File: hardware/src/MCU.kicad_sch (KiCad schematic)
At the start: 15 parts, among them U201 ESP32-C3-WROOM-02, U202 TLV1117LV33

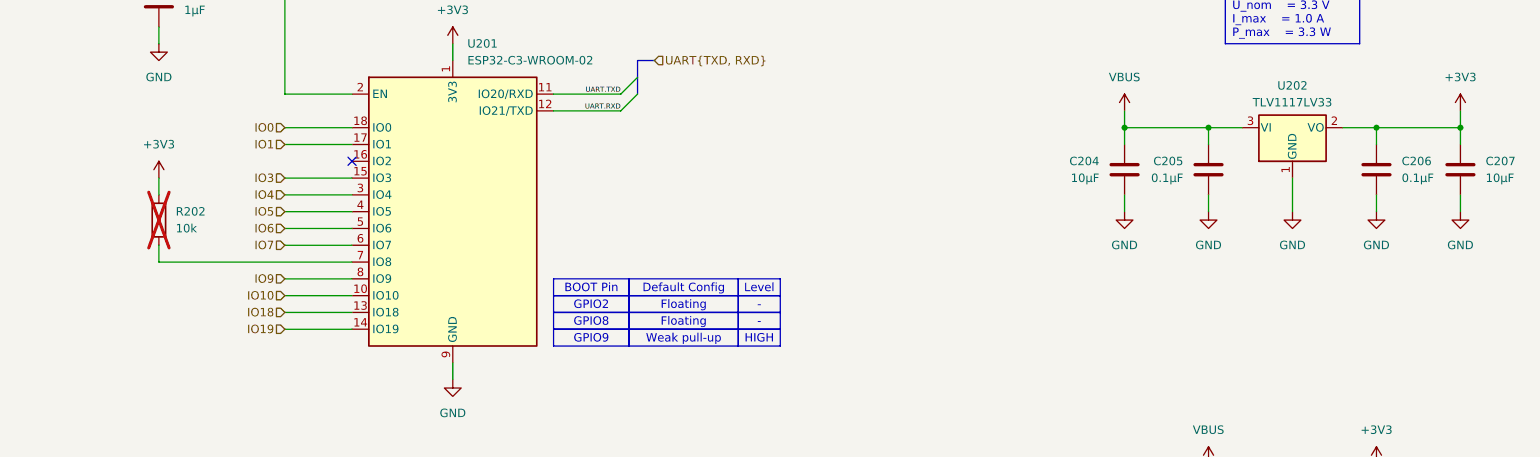
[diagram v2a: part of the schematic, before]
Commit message: Add: RTC schematic
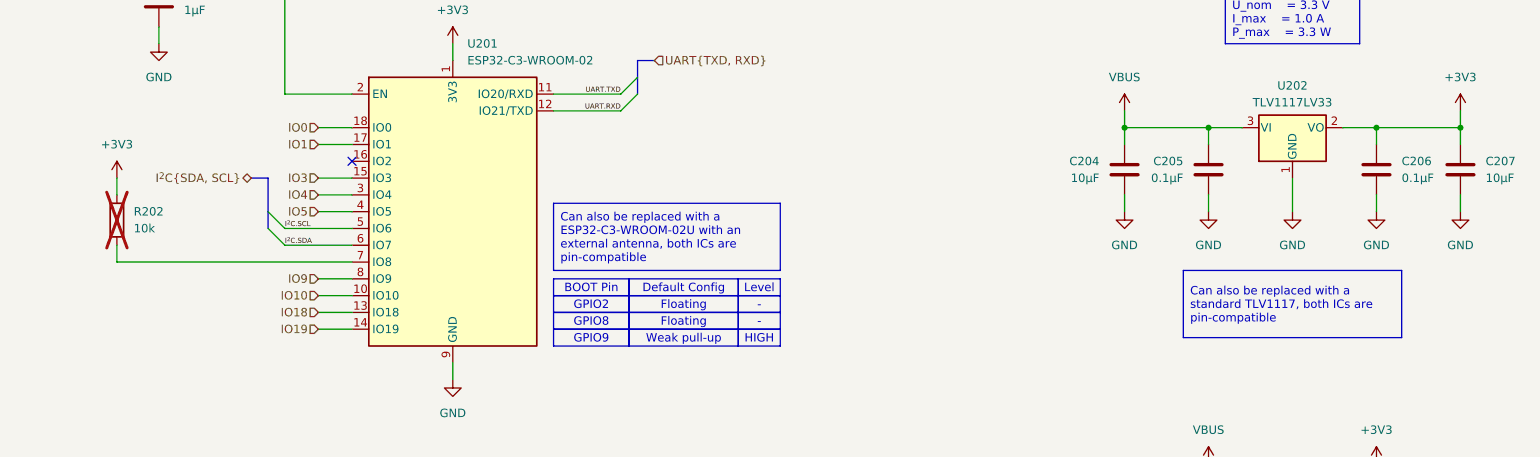
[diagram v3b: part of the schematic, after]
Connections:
- net IO6 renamed I^{2}C.SCL
- net IO7 renamed I^{2}C.SDA
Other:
- moved on the sheet: R202
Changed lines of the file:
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@@
+	)
+	(bus_entry
+		(at 60.96 78.74)
+		(size 2.54 2.54)
+		(stroke
+			(width 0)
+			(type default)
+		)
 	)
 	(bus_entry
@@
 		)
 	)
+	(bus_entry
+		(at 60.96 76.2)
+		(size 2.54 2.54)
+		(stroke
+			(width 0)
+			(type default)
+		)
+	)
 	(wire
 		(pts
@@
 	(wire
 		(pts
-			(xy 44.45 73.66) (xy 44.45 71.12)
+			(xy 38.1 73.66) (xy 38.1 71.12)
 		)
 		(stroke
@@
 		)
 	)
+	(bus
+		(pts
+			(xy 60.96 76.2) (xy 60.96 71.12)
+		)
+		(stroke
+			(width 0)
+			(type default)
+		)
+	)
 	(wire
 		(pts
@@
 		)
 	)
+	(bus
+		(pts
+			(xy 60.96 78.74) (xy 60.96 76.2)
+		)
+		(stroke
+			(width 0)
+			(type default)
+		)
+	)
 	(wire
 		(pts
@@
 	(wire
 		(pts
-			(xy 63.5 76.2) (xy 73.66 76.2)
-		)
-		(stroke
-			(width 0)
-			(type default)
-		)
-	)
-	(wire
-		(pts
-			(xy 63.5 73.66) (xy 73.66 73.66)
+			(xy 68.58 76.2) (xy 73.66 76.2)
+		)
+		(stroke
+			(width 0)
+			(type default)
+		)
+	)
+	(wire
+		(pts
+			(xy 68.58 73.66) (xy 73.66 73.66)
 		)
 		(stroke
@@
 	(wire
 		(pts
-			(xy 63.5 93.98) (xy 73.66 93.98)
+			(xy 68.58 93.98) (xy 73.66 93.98)
 		)
 		(stroke
@@
 	(wire
 		(pts
-			(xy 63.5 86.36) (xy 73.66 86.36)
+			(xy 68.58 86.36) (xy 73.66 86.36)
 		)
 		(stroke
@@
 	(wire
 		(pts
-			(xy 63.5 63.5) (xy 73.66 63.5)
+			(xy 68.58 63.5) (xy 73.66 63.5)
 		)
 		(stroke
@@
 	(wire
 		(pts
-			(xy 63.5 66.04) (xy 73.66 66.04)
+			(xy 68.58 66.04) (xy 73.66 66.04)
 		)
 		(stroke
@@
 		)
 	)
-	(wire
-		(pts
-			(xy 44.45 83.82) (xy 44.45 81.28)
+	(bus
+		(pts
+			(xy 60.96 71.12) (xy 58.42 71.12)
+		)
+		(stroke
+			(width 0)
+			(type default)
+		)
+	)
+	(wire
+		(pts
+			(xy 38.1 83.82) (xy 38.1 81.28)
 		)
 		(stroke
@@
 	(wire
 		(pts
-			(xy 63.5 91.44) (xy 73.66 91.44)
-		)
-		(stroke
-			(width 0)
-			(type default)
-		)
-	)
-	(wire
-		(pts
-			(xy 63.5 88.9) (xy 73.66 88.9)
-		)
-		(stroke
-			(width 0)
-			(type default)
-		)
-	)
-	(wire
-		(pts
-			(xy 63.5 71.12) (xy 73.66 71.12)
+			(xy 68.58 91.44) (xy 73.66 91.44)
+		)
+		(stroke
+			(width 0)
+			(type default)
+		)
+	)
+	(wire
+		(pts
+			(xy 68.58 88.9) (xy 73.66 88.9)
+		)
+		(stroke
+			(width 0)
+			(type default)
+		)
+	)
+	(wire
+		(pts
+			(xy 68.58 71.12) (xy 73.66 71.12)
 		)
 		(stroke
@@
 	(wire
 		(pts
-			(xy 73.66 83.82) (xy 44.45 83.82)
+			(xy 73.66 83.82) (xy 38.1 83.82)
 		)
 		(stroke
@@
 		)
 	)
+	(text_box "Can also be replaced with a ESP32-C3-WROOM-02U with an external antenna, both ICs are pin-compatible"
+		(exclude_from_sim no)
+		(at 104.14 74.93 0)
+		(size 34.29 10.16)
+		(stroke
+			(width 0)
+			(type default)
+		)
+		(fill
+			(type none)
+		)
+		(effects
+			(font
+				(size 1.27 1.27)
+			)
+			(justify left)
+		)
+	)
 	(text_box "U_nom	= 3.3 V\nI_max	= 1.0 A\nP_max	= 3.3 W"
 		(exclude_from_sim no)
@@
 		)
 	)
+	(text_box "Can also be replaced with a standard TLV1117, both ICs are pin-compatible"
+		(exclude_from_sim no)
+		(at 199.39 85.09 0)
+		(size 33.02 10.16)
+		(stroke
+			(width 0)
+			(type default)
+		)
+		(fill
+			(type none)
+		)
+		(effects
+			(font
+				(size 1.27 1.27)
+			)
+			(justify left)
+		)
+	)
 	(text_box "GPIO2"
 		(exclude_from_sim no)
@@
 		)
 	)
+	(label "I^{2}C.SDA"
+		(at 63.5 81.28 0)
+		(fields_autoplaced yes)
+		(effects
+			(font
+				(size 0.762 0.762)
+			)
+			(justify left bottom)
+		)
+	)
+	(label "I^{2}C.SCL"
+		(at 63.5 78.74 0)
+		(fields_autoplaced yes)
+		(effects
+			(font
+				(size 0.762 0.762)
+			)
+			(justify left bottom)
+		)
+	)
 	(label "UART.RXD"
 		(at 114.3 60.96 180)
@@
 	(hierarchical_label "IO4"
 		(shape input)
-		(at 63.5 73.66 180)
-		(fields_autoplaced yes)
-		(effects
-			(font
-				(size 1.27 1.27)
-			)
-			(justify right)
-		)
-	)
-	(hierarchical_label "IO6"
-		(shape input)
-		(at 63.5 78.74 180)
+		(at 68.58 73.66 180)
 		(fields_autoplaced yes)
 		(effects
@@
 	(hierarchical_label "IO9"
 		(shape input)
-		(at 63.5 86.36 180)
+		(at 68.58 86.36 180)
 		(fields_autoplaced yes)
 		(effects
@@
 	(hierarchical_label "IO18"
 		(shape input)
-		(at 63.5 91.44 180)
+		(at 68.58 91.44 180)
 		(fields_autoplaced yes)
 		(effects
@@
 	(hierarchical_label "IO1"
 		(shape input)
-		(at 63.5 66.04 180)
+		(at 68.58 66.04 180)
 		(fields_autoplaced yes)
 		(effects
@@
 	(hierarchical_label "IO19"
 		(shape input)
-		(at 63.5 93.98 180)
+		(at 68.58 93.98 180)
 		(fields_autoplaced yes)
 		(effects
@@
 	(hierarchical_label "IO0"
 		(shape input)
-		(at 63.5 63.5 180)
+		(at 68.58 63.5 180)
 		(fields_autoplaced yes)
 		(effects
@@
 	(hierarchical_label "IO3"
 		(shape input)
-		(at 63.5 71.12 180)
+		(at 68.58 71.12 180)
 		(fields_autoplaced yes)
 		(effects
@@
 		)
 	)
-	(hierarchical_label "IO7"
-		(shape input)
-		(at 63.5 81.28 180)
+	(hierarchical_label "I^{2}C{SDA, SCL}"
+		(shape bidirectional)
+		(at 58.42 71.12 180)
 		(fields_autoplaced yes)
 		(effects
@@
 	(hierarchical_label "IO5"
 		(shape input)
-		(at 63.5 76.2 180)
+		(at 68.58 76.2 180)
 		(fields_autoplaced yes)
 		(effects
@@
 	(hierarchical_label "IO10"
 		(shape input)
-		(at 63.5 88.9 180)
+		(at 68.58 88.9 180)
 		(fields_autoplaced yes)
 		(effects
@@
 	(symbol
 		(lib_id "power:+3V3")
-		(at 44.45 71.12 0)
+		(at 38.1 71.12 0)
 		(mirror y)
 		(unit 1)
@@
 		(fields_autoplaced yes)
 		(property "Reference" "#PWR0207"
-			(at 44.45 74.93 0)
+			(at 38.1 74.93 0)
 			(effects
 				(font
@@
 		)
 		(property "Value" "+3V3"
-			(at 44.45 66.04 0)
+			(at 38.1 66.04 0)
 			(effects
 				(font
@@
 		)
 		(property "Footprint" ""
-			(at 44.45 71.12 0)
+			(at 38.1 71.12 0)
 			(effects
 				(font
@@
 		)
 		(property "Datasheet" ""
-			(at 44.45 71.12 0)
+			(at 38.1 71.12 0)
 			(effects
 				(font
@@
 		)
 		(property "Description" "Power symbol creates a global label with name \"+3V3\""
-			(at 44.45 71.12 0)
+			(at 38.1 71.12 0)
 			(effects
 				(font
@@
 	(symbol
 		(lib_id "Device:R")
-		(at 44.45 77.47 0)
+		(at 38.1 77.47 0)
 		(unit 1)
 		(exclude_from_sim no)
@@
 		(fields_autoplaced yes)
 		(property "Reference" "R202"
-			(at 46.99 76.1999 0)
+			(at 40.64 76.1999 0)
 			(effects
 				(font
@@
 		)
 		(property "Value" "10k"
-			(at 46.99 78.7399 0)
+			(at 40.64 78.7399 0)
 			(effects
 				(font
@@
 		)
 		(property "Footprint" ""
-			(at 42.672 77.47 90)
+			(at 36.322 77.47 90)
 			(effects
 				(font
@@
 		)
 		(property "Datasheet" "~"
-			(at 44.45 77.47 0)
+			(at 38.1 77.47 0)
 			(effects
 				(font
@@
 		)
 		(property "Description" "Resistor"
-			(at 44.45 77.47 0)
-			(effects
-				(font
+			(at 38.1 77.47 0)
+			(effects
+				(font

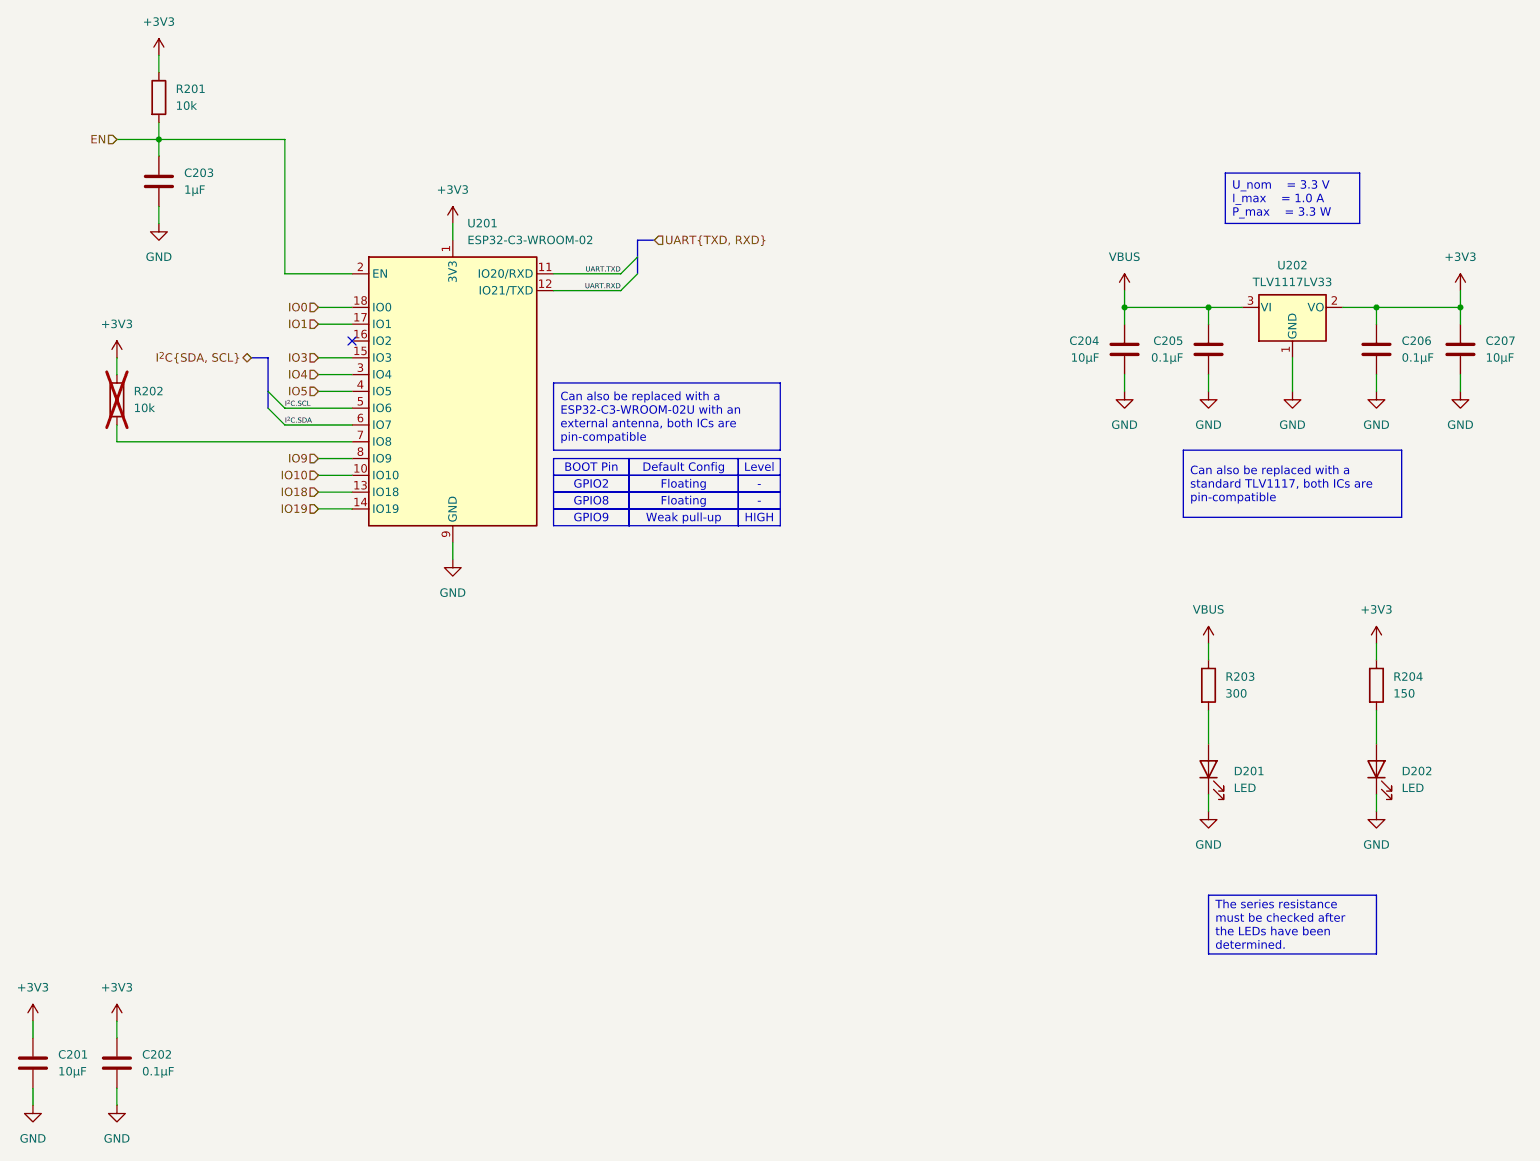
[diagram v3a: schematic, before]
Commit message: Mod: RTC GPIOs
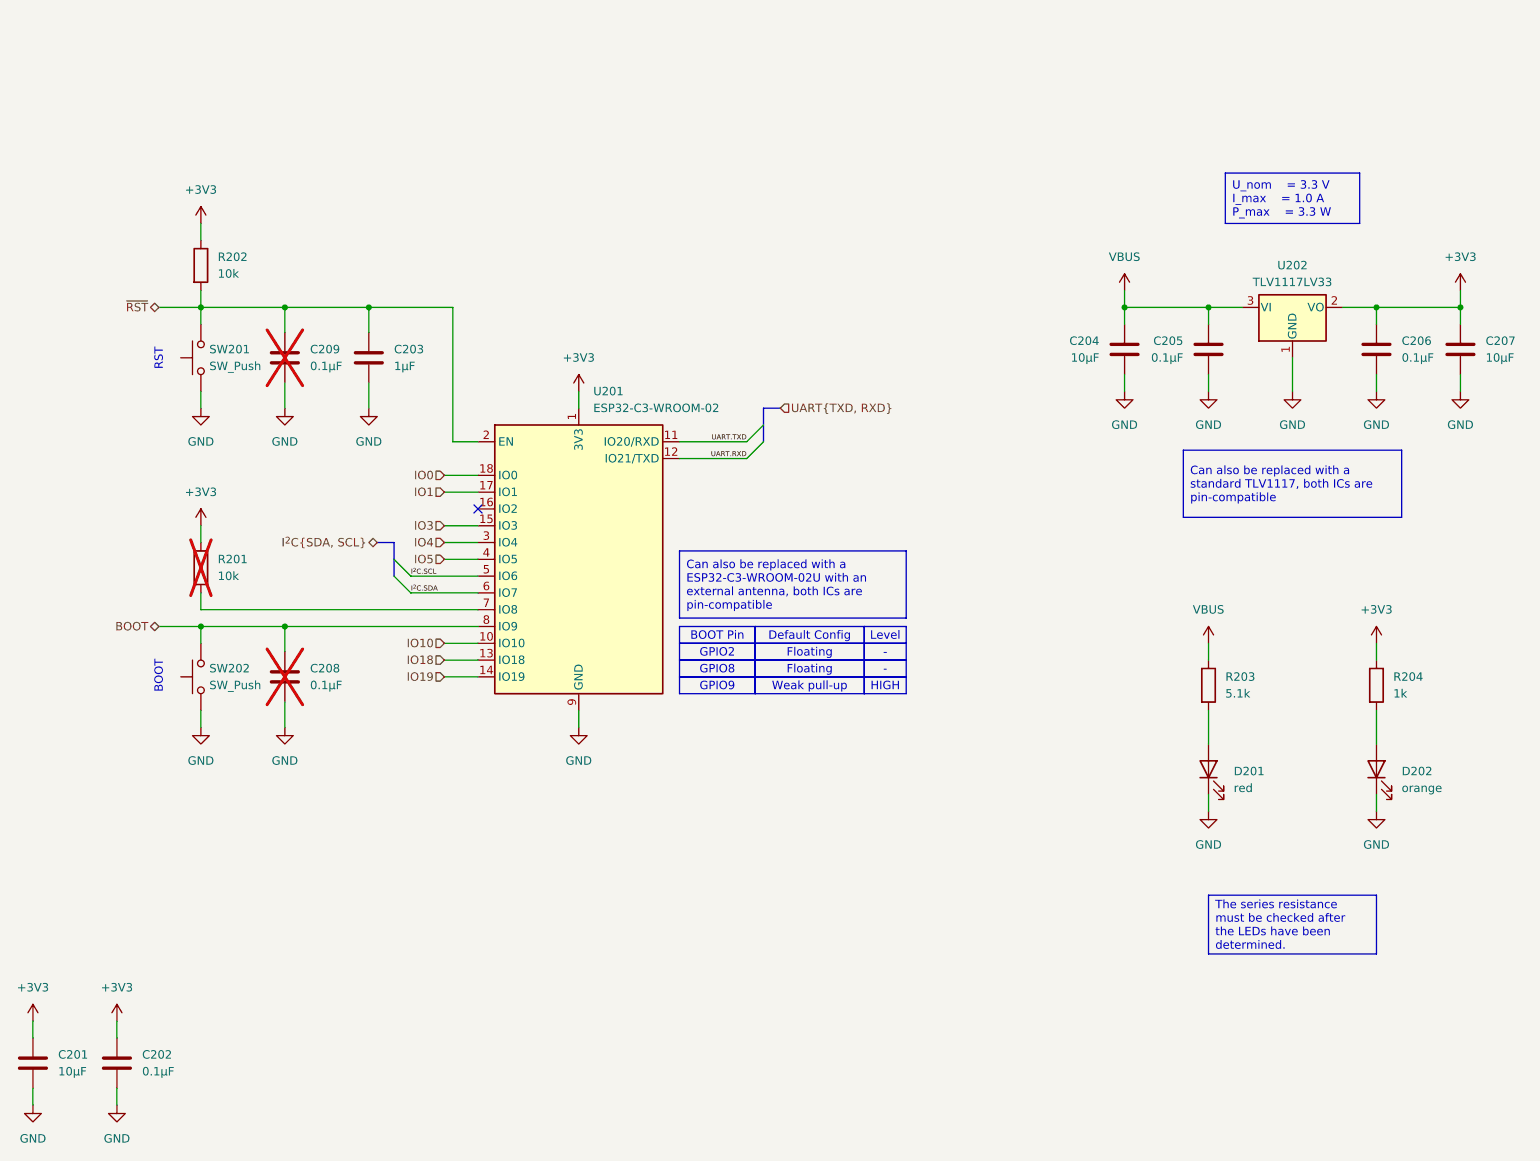
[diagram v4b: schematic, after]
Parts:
- added C208, C209: 0.1µF, symbol Device:C
- added SW201, SW202: SW_Push, symbol Switch:SW_Push
- D201: value LED -> red
- D202: value LED -> orange
- R203: value 300 -> 5.1k
- R204: value 150 -> 1k
- renumbered R202 to R201, R201 to R202
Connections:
- net GND: now also C208.2, C209.2, SW201.1, SW202.1
- net EN renamed ~{RST}
- net ~{RST}: now also C209.1, SW201.2
- net IO9 renamed BOOT
- net BOOT: now also C208.1, SW202.2
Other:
- note added: "BOOT"
- note added: "RST"
- moved on the sheet: C203, R201, R202, U201
